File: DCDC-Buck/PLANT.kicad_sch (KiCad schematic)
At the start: 7 parts, among them IC2 IR2117, Q1 IRF740

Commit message: Finishing SCH document.
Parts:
- removed C1: C, symbol Device:C
- removed R1, R2: R, Diode_THT:D_DO-41_SOD81_P10.16mm_Horizontal, symbol Device:R
- added C10, C11: 4.7uF, Capacitor_THT:C_Radial_D5.0mm_H7.0mm_P2.00mm, symbol Device:C_Polarized
- added C12: 470nF, Capacitor_THT:C_Rect_L13.0mm_W4.0mm_P10.00mm_FKS3_FKP3_MKS4, symbol Device:C
- added C9: 100nF, symbol Device:C
- added D3: 1N4007, Diode_THT:D_DO-41_SOD81_P10.16mm_Horizontal, symbol Diode:1N4007
- added D4: UF4007, Diode_THT:D_DO-41_SOD81_P10.16mm_Horizontal, symbol Diode:1N4007
- added D5: MBR1545CT, Package_TO_SOT_THT:TO-220-3_Vertical, symbol Diode:1N4007
- added R25, R26: 100kR, Resistor_THT:R_Axial_DIN0207_L6.3mm_D2.5mm_P7.62mm_Horizontal, symbol Device:R
- C2: value C -> 100uF; footprint (none) -> Capacitor_THT:CP_Radial_Tantal_D5.0mm_P5.00mm; Link (none) -> https://www.multcomercial.com.br/capacitor-tantalo-100uf-35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; Voltage (none) -> 35V
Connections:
- net +15V: now also IC2.1 (VCC), C11.1, C9.1, D3.2 (A)
- net +Vin: now also C10.1
- net GND: now also IC2.3 (COM), C10.2, C11.2, C9.2, D5.1 (A), D5.3 (A)
- net Vpwm: now also IC2.2 (IN)
- net at Q1.1 (G): now also D4.2 (A), R25.2, R26.1
- net at L1.1, Q1.3 (S): now also IC2.6 (VS), C12.2, D5.2 (K), R25.1
- net at IC2.7 (HO): now also D4.1 (K), R26.2
- net at IC2.8 (VB): now also C12.1, D3.1 (K)
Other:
- moved on the sheet: C2, IC2, L1, Q1

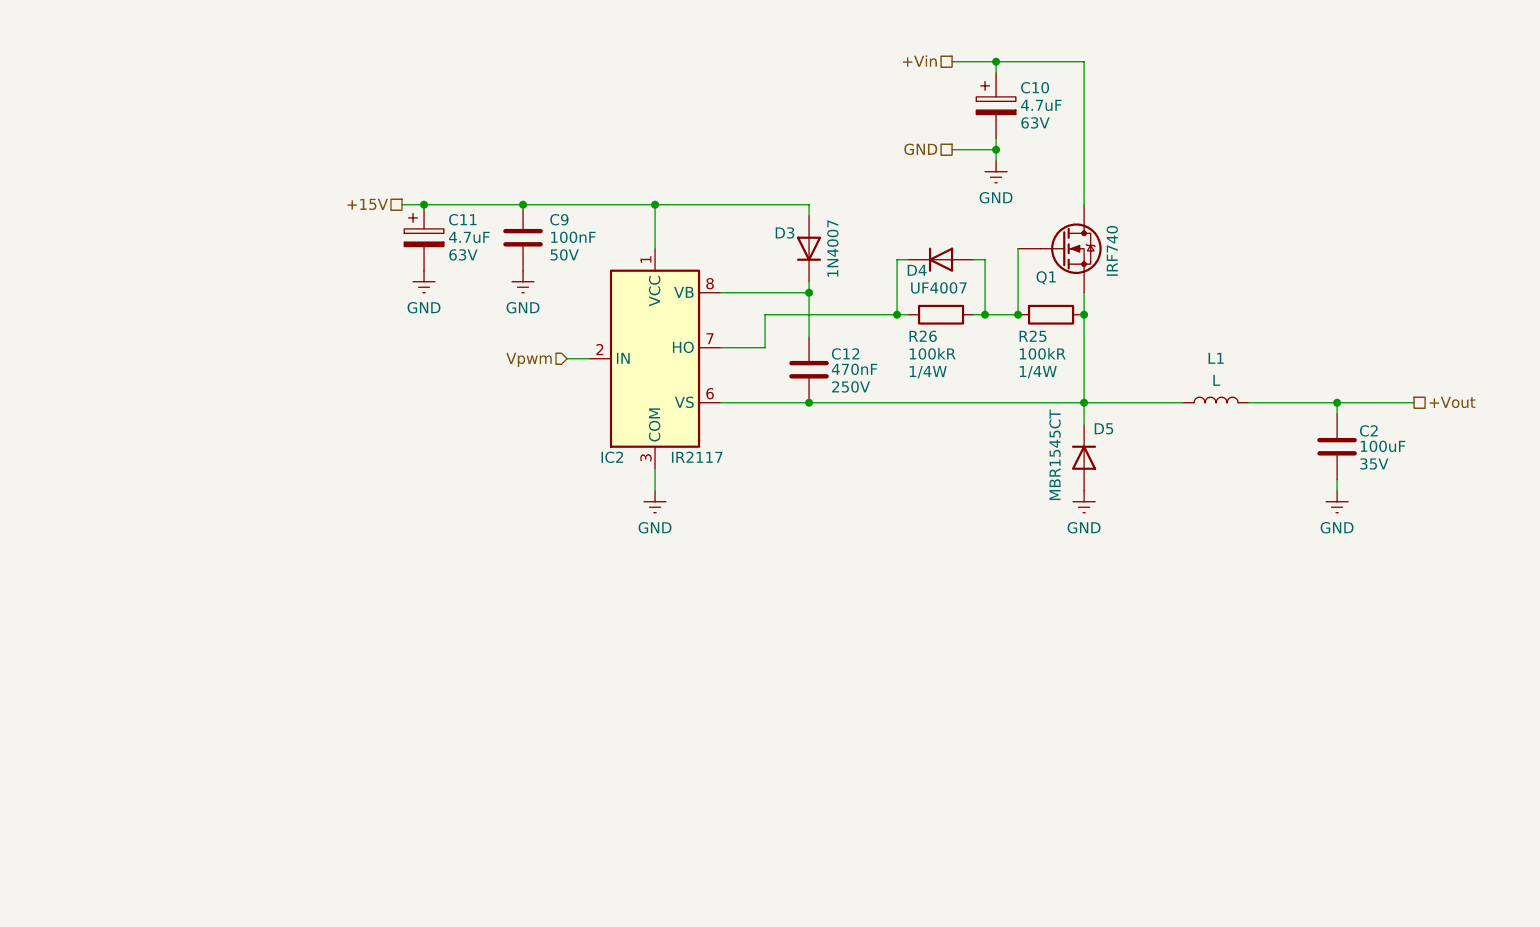
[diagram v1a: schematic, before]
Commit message: Finishing PCB design with 2 layers.
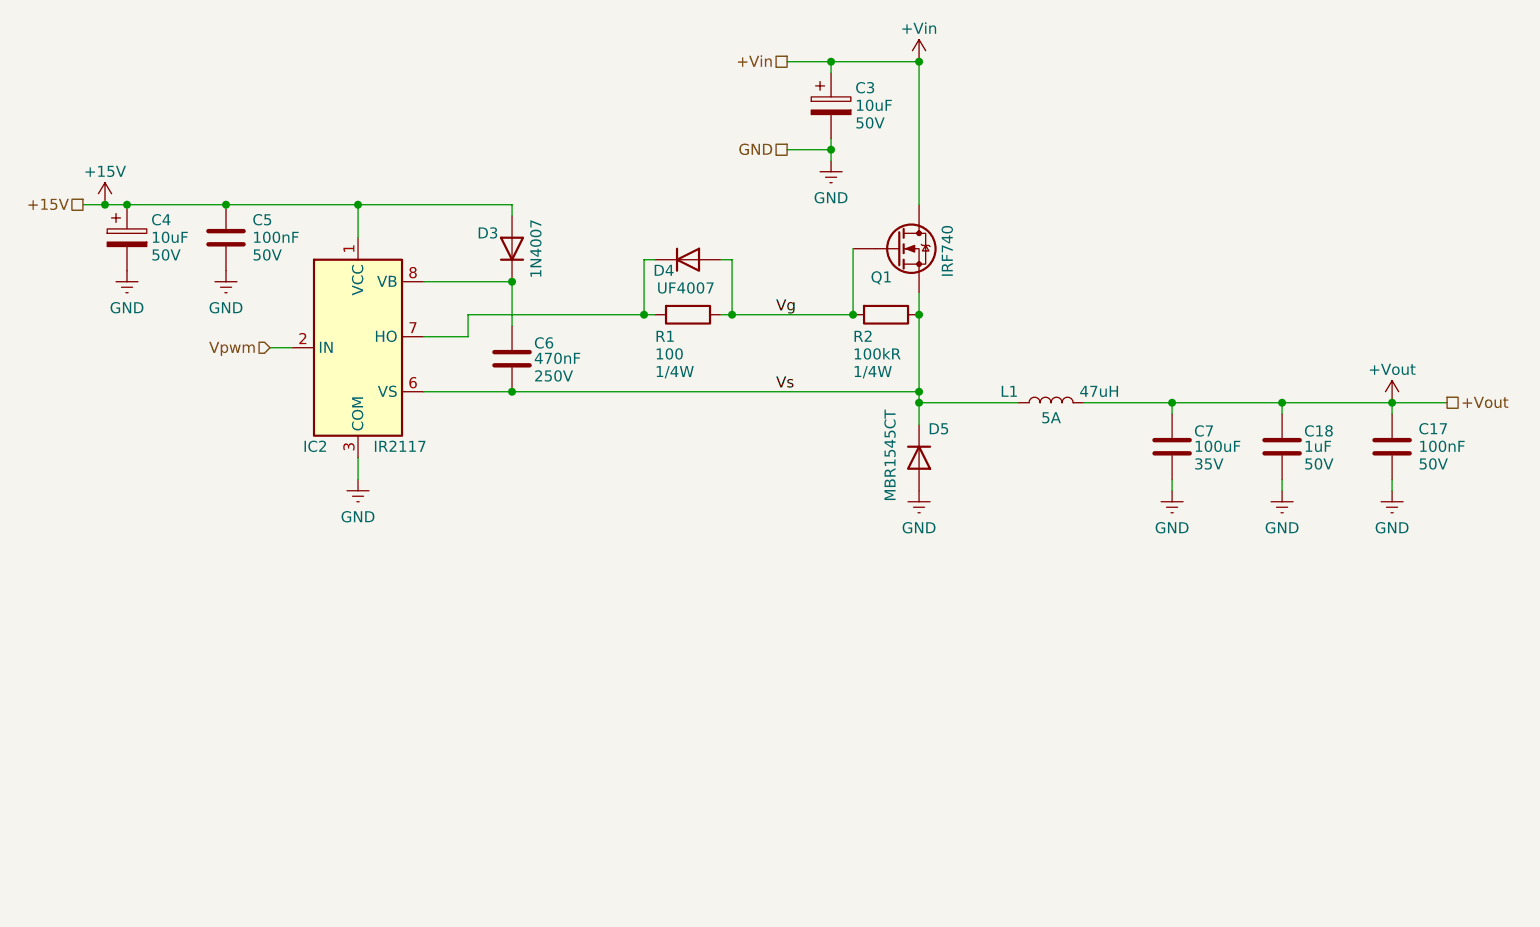
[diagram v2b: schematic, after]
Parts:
- removed C10: 4.7uF, Capacitor_THT:C_Radial_D5.0mm_H7.0mm_P2.00mm, symbol Device:C_Polarized
- added C17: 100nF, Capacitor_THT:C_Disc_D3.0mm_W2.0mm_P2.50mm, symbol Device:C
- added C18: 1uF, Capacitor_THT:CP_Radial_Tantal_D5.0mm_P5.00mm, symbol Device:C
- added C3: 10uF, Capacitor_THT:C_Radial_D6.3mm_H11.0mm_P2.50mm, symbol Device:C_Polarized
- C4: renamed from C11; value 4.7uF -> 10uF; footprint Capacitor_THT:C_Radial_D5.0mm_H7.0mm_P2.00mm -> Capacitor_THT:C_Radial_D6.3mm_H11.0mm_P2.50mm; Link https://www.multcomercial.com.br/capacitor-eletrolitico-4-7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 -> https://www.multcomercial.com.br/capacitor-eletrolitico-de-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; Voltage 63V -> 50V
- C5: renamed from C9; footprint (none) -> Capacitor_THT:C_Disc_D3.0mm_W2.0mm_P2.50mm; Link https://www.multcomercial.com.br/capacitor-multicamada-100k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 -> https://www.multcomercial.com.br/capacitor-ceramico-disco-1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
- C7: renamed from C2; footprint Capacitor_THT:CP_Radial_Tantal_D5.0mm_P5.00mm -> Capacitor_THT:CP_Radial_Tantal_D8.0mm_P5.00mm
- L1: value L -> 47uH; footprint Package_TO_SOT_THT:TO-220-3_Vertical -> Inductor_THT:L_Toroid_Vertical_L16.0mm_W8.0mm_P7.62mm; Current (none) -> 5A
- R1: renamed from R26; value 100kR -> 100
- renumbered C12 to C6, R25 to R2
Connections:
- net +Vin: now also C3.1
- net +Vout: now also C17.1, C18.1
- net GND: now also C17.2, C18.2, C3.2
- net Vg: now reaches D4.2 (A), Q1.1 (G), R1.1, R2.2
- net Vs: now reaches C6.2, D5.2 (K), IC2.6 (VS), L1.1, Q1.3 (S), R2.1
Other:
- moved on the sheet: C4, C5, C6, C7, D3, D4, D5, IC2, L1, Q1, R1, R2

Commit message: FInishing BOM and PCB.
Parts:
- R1: value 100 -> 100R
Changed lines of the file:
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@@
 			)
 		)
-		(property "Value" "100"
+		(property "Value" "100R"
 			(at 137.16 101.092 90)
 			(show_name no)

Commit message: Editing some bug fixes in controller and plant.
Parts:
- C18: value 1uF -> 100uF; footprint Capacitor_THT:CP_Radial_Tantal_D5.0mm_P5.00mm -> Capacitor_THT:CP_Radial_Tantal_D8.0mm_P5.00mm; Link https://www.multcomercial.com.br/capacitor-multicamada-1uf-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 -> https://www.multcomercial.com.br/capacitor-tantalo-100uf-35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; Voltage 50V -> 35V
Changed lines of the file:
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@@
+	)
+	(symbol
+		(lib_id "Device:C")
+		(at 209.55 111.76 0)
+		(unit 1)
+		(body_style 1)
+		(exclude_from_sim no)
+		(in_bom yes)
+		(on_board yes)
+		(in_pos_files yes)
+		(dnp no)
+		(property "Reference" "C18"
+			(at 212.09 109.982 0)
+			(show_name no)
+			(do_not_autoplace no)
+			(effects
+				(font
+					(size 1.27 1.27)
+				)
+				(justify left)
+			)
+		)
+		(property "Value" "100uF"
+			(at 212.09 111.7599 0)
+			(show_name no)
+			(do_not_autoplace no)
+			(effects
+				(font
+					(size 1.27 1.27)
+				)
+				(justify left)
+			)
+		)
+		(property "Footprint" "Capacitor_THT:CP_Radial_Tantal_D8.0mm_P5.00mm"
+			(at 210.5152 115.57 0)
+			(hide yes)
+			(show_name no)
+			(do_not_autoplace no)
+			(effects
+				(font
+					(size 1.27 1.27)
+				)
+			)
+		)
+		(property "Datasheet" ""
+			(at 209.55 111.76 0)
+			(hide yes)
+			(show_name no)
+			(do_not_autoplace no)
+			(effects
+				(font
+					(size 1.27 1.27)
+				)
+			)
+		)
+		(property "Description" "Unpolarized capacitor"
+			(at 209.55 111.76 0)
+			(hide yes)
+			(show_name no)
+			(do_not_autoplace no)
+			(effects
+				(font
+					(size 1.27 1.27)
+				)
+			)
+		)
+		(property "Voltage" "35V"
+			(at 212.09 113.792 0)
+			(show_name no)
+			(do_not_autoplace no)
+			(effects
+				(font
+					(size 1.27 1.27)
+				)
+				(justify left)
+			)
+		)
+		(property "Link" "https://www.multcomercial.com.br/capacitor-tantalo-100uf-35v-cod-loja-3637.html"
+			(at 209.55 111.76 0)
+			(hide yes)
+			(show_name no)
+			(do_not_autoplace no)
+			(effects
+				(font
+					(size 1.27 1.27)
+				)
+			)
+		)
+		(pin "2"
+		)
+		(pin "1"
+		)
+		(instances
+			(project "DCDC-Buck"
+				(path "/959e3d1c-01d0-4c7d-bf19-165b598aa596/158ee772-3f55-4806-ae2f-18e95f09a57b"
+					(reference "C18")
+					(unit 1)
+				)
+			)
+		)
 	)
 	(symbol
@@
 					(unit 1)
 				)
-			)
-		)
-	)
-	(symbol
-		(lib_id "Device:C")
-		(at 209.55 111.76 0)
-		(unit 1)
-		(body_style 1)
-		(exclude_from_sim no)
-		(in_bom yes)
-		(on_board yes)
-		(in_pos_files yes)
-		(dnp no)
-		(property "Reference" "C18"
-			(at 212.09 109.982 0)
-			(show_name no)
-			(do_not_autoplace no)
-			(effects
-				(font
-					(size 1.27 1.27)
-				)
-				(justify left)
-			)
-		)
-		(property "Value" "1uF"
-			(at 212.09 111.7599 0)
-			(show_name no)
-			(do_not_autoplace no)
-			(effects
-				(font
-					(size 1.27 1.27)
-				)
-				(justify left)
-			)
-		)
-		(property "Footprint" "Capacitor_THT:CP_Radial_Tantal_D5.0mm_P5.00mm"
-			(at 210.5152 115.57 0)
-			(hide yes)
-			(show_name no)
-			(do_not_autoplace no)
-			(effects
-				(font
-					(size 1.27 1.27)
-				)
-			)
-		)
-		(property "Datasheet" ""
-			(at 209.55 111.76 0)
-			(hide yes)
-			(show_name no)
-			(do_not_autoplace no)
-			(effects
-				(font
-					(size 1.27 1.27)
-				)
-			)
-		)
-		(property "Description" "Unpolarized capacitor"
-			(at 209.55 111.76 0)
-			(hide yes)
-			(show_name no)
-			(do_not_autoplace no)
-			(effects
-				(font
-					(size 1.27 1.27)
-				)
-			)
-		)
-		(property "Voltage" "50V"
-			(at 212.09 113.792 0)
-			(show_name no)
-			(do_not_autoplace no)
-			(effects
-				(font
-					(size 1.27 1.27)
-				)
-				(justify left)
-			)
-		)
-		(property "Link" "https://www.multcomercial.com.br/capacitor-multicamada-1uf-50v-cod-loja-3384.html"
-			(at 209.55 111.76 0)
-			(hide yes)
-			(show_name no)
-			(do_not_autoplace no)
-			(effects
-				(font
-					(size 1.27 1.27)
-				)
-			)
-		)
-		(pin "2"
-		)
-		(pin "1"
-		)
-		(instances
-			(project "DCDC-Buck"
-				(path "/959e3d1c-01d0-4c7d-bf19-165b598aa596/158ee772-3f55-4806-ae2f-18e95f09a57b"
-					(reference "C18")
-					(unit 1)
-				)

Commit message: Changing 1nF capacitor and buck-plant inductor footprints. Ready to release v1.0.1 (bug-fixes).
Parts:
- L1: footprint Inductor_THT:L_Toroid_Vertical_L16.0mm_W8.0mm_P7.62mm -> Inductor_THT:L_Toroid_Vertical_L25.4mm_W14.7mm_P12.20mm_Vishay_TJ5
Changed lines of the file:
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@@
 			)
 		)
-		(property "Footprint" "Inductor_THT:L_Toroid_Vertical_L16.0mm_W8.0mm_P7.62mm"
+		(property "Footprint" "Inductor_THT:L_Toroid_Vertical_L25.4mm_W14.7mm_P12.20mm_Vishay_TJ5"
 			(at 182.88 106.68 0)
 			(hide yes)
